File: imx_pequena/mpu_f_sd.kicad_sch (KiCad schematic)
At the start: 1 part, among them U1 MCIMX6Z0DVM09AB

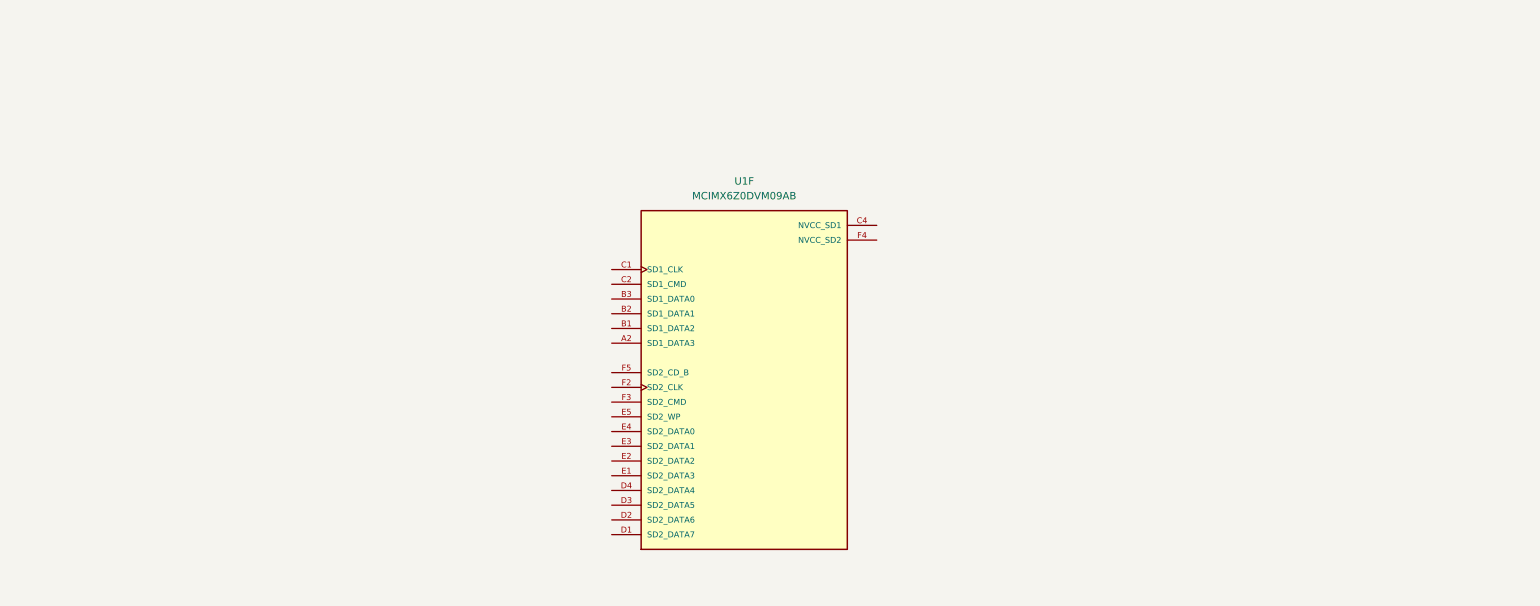
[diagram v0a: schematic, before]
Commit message: SD card + pinot files
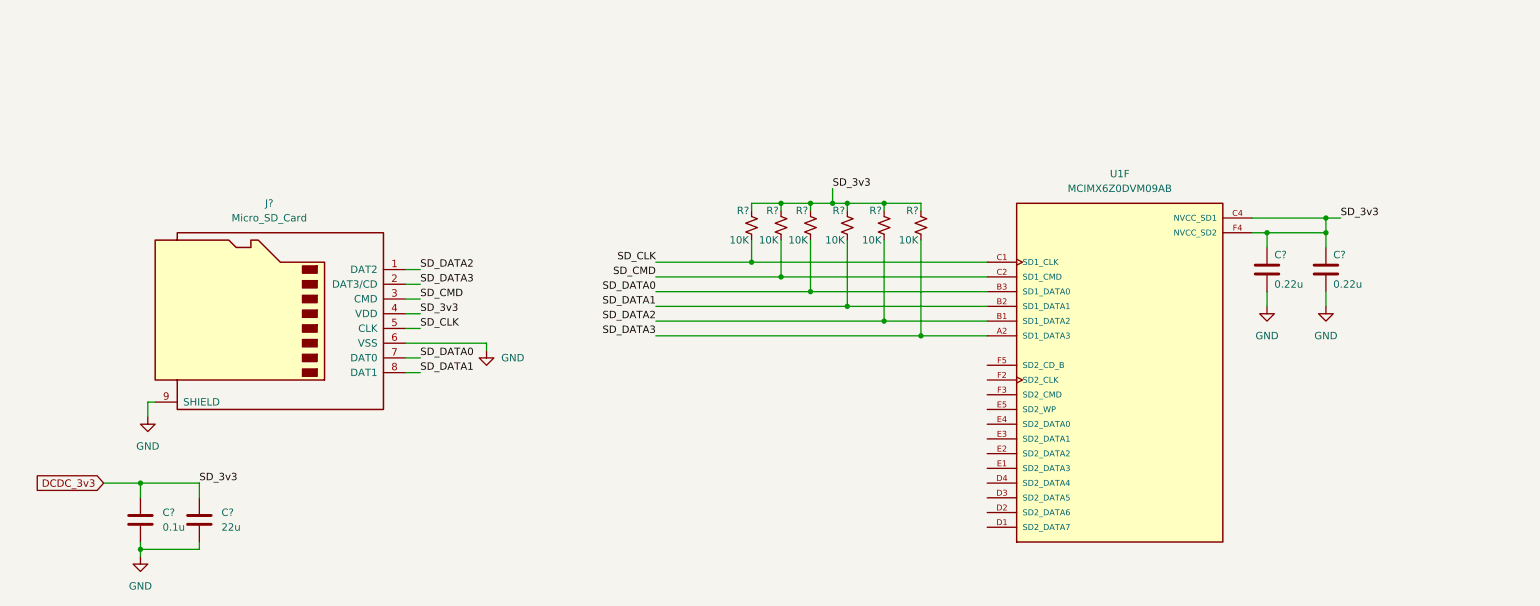
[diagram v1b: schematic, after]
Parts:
- added C? (x2): 0.22u, symbol Device:C
- added C?: 22u, symbol Device:C
- added C?: 0.1u, symbol Device:C
- added J?: Micro_SD_Card, symbol Connector:Micro_SD_Card
- added R? (x6): 10K, symbol Device:R_Small_US
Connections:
- net SD_DATA3: now reaches U1.A2 (SD1_DATA3)
- net SD_DATA3: now also J?.2 (DAT3/CD), R?.2
- net SD_DATA2: now reaches U1.B1 (SD1_DATA2)
- net SD_DATA2: now also J?.1 (DAT2), R?.2
- net SD_DATA1: now reaches U1.B2 (SD1_DATA1)
- net SD_DATA1: now also J?.8 (DAT1), R?.2
- net SD_DATA0: now reaches U1.B3 (SD1_DATA0)
- net SD_DATA0: now also J?.7 (DAT0), R?.2
- net SD_CLK: now reaches U1.C1 (SD1_CLK)
- net SD_CLK: now also J?.5 (CLK), R?.2
- net SD_CMD: now reaches U1.C2 (SD1_CMD)
- net SD_CMD: now also J?.3 (CMD), R?.2
- net DCDC_3v3: now reaches U1.C4 (NVCC_SD1)
- net DCDC_3v3: now also U1.F4 (NVCC_SD2), C?.1, C?.1, C?.1, C?.1, J?.4 (VDD), R?.1, R?.1, R?.1, R?.1, R?.1, R?.1
- new net GND: C?.2, C?.2, C?.2, C?.2, J?.6 (VSS), J?.9 (SHIELD)
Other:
- moved on the sheet: U1F

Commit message: Power Update
Added 3v3 and 1.35V switchers
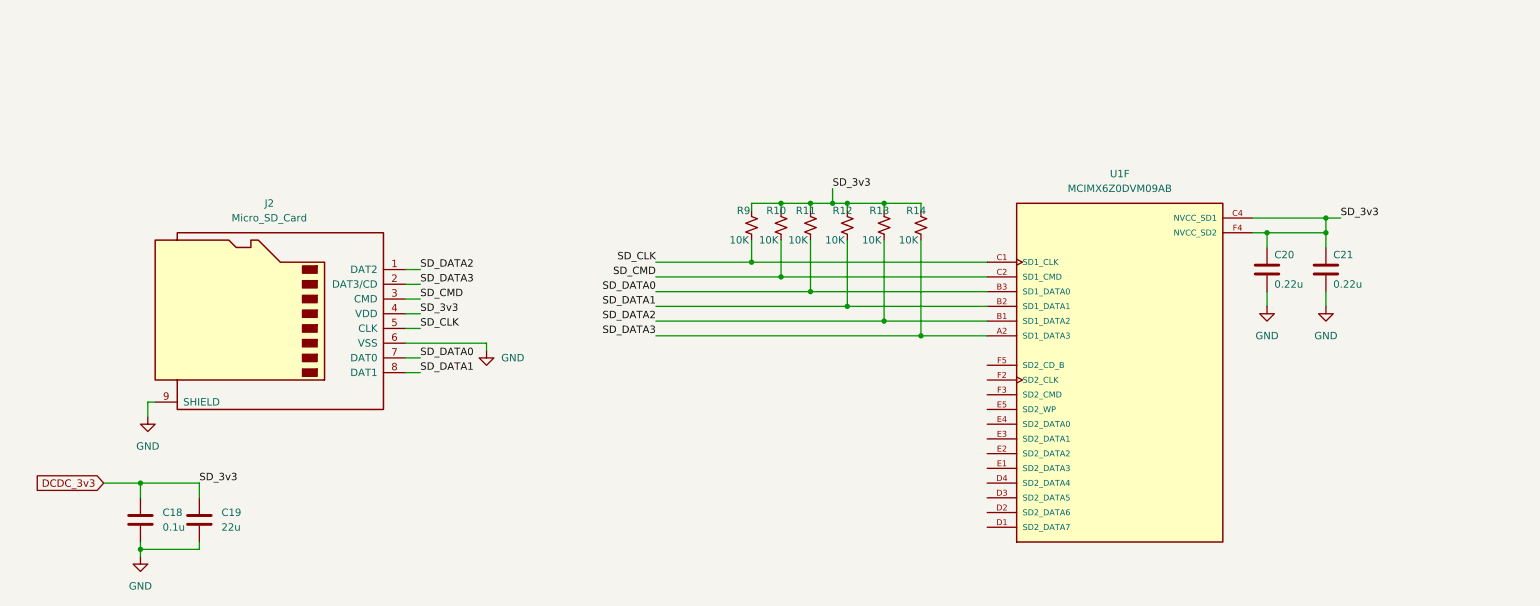
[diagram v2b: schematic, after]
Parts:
- gave numbers to parts that had none: 11
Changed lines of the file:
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@@
   (symbol (lib_id "Device:C") (at 245.11 62.23 0) (unit 1)
     (in_bom yes) (on_board yes)
-    (property "Reference" "C?" (id 0) (at 246.38 59.69 0)
+    (property "Reference" "C21" (id 0) (at 246.38 59.69 0)
       (effects (font (size 1.27 1.27)) (justify left))
     )
@@
   (symbol (lib_id "Device:R_Small_US") (at 156.21 54.61 0) (unit 1)
     (in_bom yes) (on_board yes)
-    (property "Reference" "R?" (id 0) (at 153.67 52.07 0)
+    (property "Reference" "R11" (id 0) (at 153.67 52.07 0)
       (effects (font (size 1.27 1.27)) (justify left))
     )
@@
   (symbol (lib_id "Device:R_Small_US") (at 146.05 54.61 0) (unit 1)
     (in_bom yes) (on_board yes)
-    (property "Reference" "R?" (id 0) (at 143.51 52.07 0)
+    (property "Reference" "R9" (id 0) (at 143.51 52.07 0)
       (effects (font (size 1.27 1.27)) (justify left))
     )
@@
   (symbol (lib_id "Device:R_Small_US") (at 175.26 54.61 0) (unit 1)
     (in_bom yes) (on_board yes)
-    (property "Reference" "R?" (id 0) (at 172.72 52.07 0)
+    (property "Reference" "R14" (id 0) (at 172.72 52.07 0)
       (effects (font (size 1.27 1.27)) (justify left))
     )
@@
   (symbol (lib_id "power:GND") (at 100.33 76.2 0) (unit 1)
     (in_bom yes) (on_board yes) (fields_autoplaced)
-    (property "Reference" "#PWR?" (id 0) (at 100.33 82.55 0)
+    (property "Reference" "#PWR0118" (id 0) (at 100.33 82.55 0)
       (effects (font (size 1.27 1.27)) hide)
     )
@@
   (symbol (lib_id "Device:C") (at 50.8 105.41 0) (unit 1)
     (in_bom yes) (on_board yes) (fields_autoplaced)
-    (property "Reference" "C?" (id 0) (at 54.61 104.1399 0)
+    (property "Reference" "C19" (id 0) (at 54.61 104.1399 0)
       (effects (font (size 1.27 1.27)) (justify left))
     )
@@
   (symbol (lib_id "Device:C") (at 234.95 62.23 0) (unit 1)
     (in_bom yes) (on_board yes)
-    (property "Reference" "C?" (id 0) (at 236.22 59.69 0)
+    (property "Reference" "C20" (id 0) (at 236.22 59.69 0)
       (effects (font (size 1.27 1.27)) (justify left))
     )
@@
   (symbol (lib_id "Connector:Micro_SD_Card") (at 63.5 69.85 0) (mirror y) (unit 1)
     (in_bom yes) (on_board yes) (fields_autoplaced)
-    (property "Reference" "J?" (id 0) (at 62.865 50.8 0))
+    (property "Reference" "J2" (id 0) (at 62.865 50.8 0))
     (property "Value" "Micro_SD_Card" (id 1) (at 62.865 53.34 0))
     (property "Footprint" "" (id 2) (at 34.29 62.23 0)
@@
   (symbol (lib_id "power:GND") (at 245.11 68.58 0) (unit 1)
     (in_bom yes) (on_board yes) (fields_autoplaced)
-    (property "Reference" "#PWR?" (id 0) (at 245.11 74.93 0)
+    (property "Reference" "#PWR0119" (id 0) (at 245.11 74.93 0)
       (effects (font (size 1.27 1.27)) hide)
     )
@@
   (symbol (lib_id "power:GND") (at 40.64 111.76 0) (unit 1)
     (in_bom yes) (on_board yes) (fields_autoplaced)
-    (property "Reference" "#PWR?" (id 0) (at 40.64 118.11 0)
+    (property "Reference" "#PWR0117" (id 0) (at 40.64 118.11 0)
       (effects (font (size 1.27 1.27)) hide)
     )
@@
   (symbol (lib_id "power:GND") (at 41.91 87.63 0) (unit 1)
     (in_bom yes) (on_board yes) (fields_autoplaced)
-    (property "Reference" "#PWR?" (id 0) (at 41.91 93.98 0)
+    (property "Reference" "#PWR0116" (id 0) (at 41.91 93.98 0)
       (effects (font (size 1.27 1.27)) hide)
     )
@@
   (symbol (lib_id "Device:C") (at 40.64 105.41 0) (unit 1)
     (in_bom yes) (on_board yes) (fields_autoplaced)
-    (property "Reference" "C?" (id 0) (at 44.45 104.1399 0)
+    (property "Reference" "C18" (id 0) (at 44.45 104.1399 0)
       (effects (font (size 1.27 1.27)) (justify left))
     )
@@
   (symbol (lib_id "power:GND") (at 234.95 68.58 0) (unit 1)
     (in_bom yes) (on_board yes) (fields_autoplaced)
-    (property "Reference" "#PWR?" (id 0) (at 234.95 74.93 0)
+    (property "Reference" "#PWR0120" (id 0) (at 234.95 74.93 0)
       (effects (font (size 1.27 1.27)) hide)
     )
@@
   (symbol (lib_id "Device:R_Small_US") (at 168.91 54.61 0) (unit 1)
     (in_bom yes) (on_board yes)
-    (property "Reference" "R?" (id 0) (at 166.37 52.07 0)
+    (property "Reference" "R13" (id 0) (at 166.37 52.07 0)
       (effects (font (size 1.27 1.27)) (justify left))
     )
@@
   (symbol (lib_id "Device:R_Small_US") (at 162.56 54.61 0) (unit 1)
     (in_bom yes) (on_board yes)
-    (property "Reference" "R?" (id 0) (at 160.02 52.07 0)
+    (property "Reference" "R12" (id 0) (at 160.02 52.07 0)
       (effects (font (size 1.27 1.27)) (justify left))
     )
@@
   (symbol (lib_id "Device:R_Small_US") (at 151.13 54.61 0) (unit 1)
     (in_bom yes) (on_board yes)
-    (property "Reference" "R?" (id 0) (at 148.59 52.07 0)
-      (effects (font (size 1.27 1.27)) (justify left))
-    )
+    (property "Reference" "R10" (id 0) (at 148.59 52.07 0)
+      (effects (font (size 1.27 1.27)) (justify left))
+    )

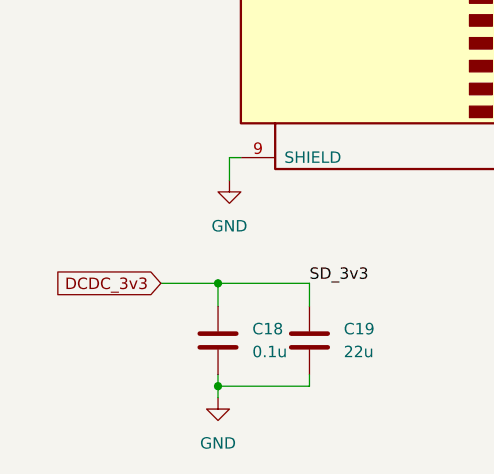
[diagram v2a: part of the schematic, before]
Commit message: Cleaned up NVCC pins
Added 3v3 connections + decoupling caps to NVcc pins
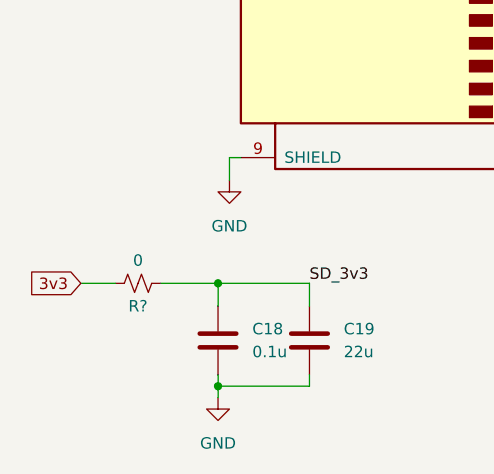
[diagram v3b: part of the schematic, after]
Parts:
- added R?: 0, symbol Device:R_Small_US
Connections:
- net DCDC_3v3 renamed SD_3v3
- net SD_3v3: now also R?.1
- new net 3v3: R?.2
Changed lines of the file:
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@@
+    (stroke (width 0) (type default) (color 0 0 0 0))
+  )
+  (wire (pts (xy 29.21 99.06) (xy 25.4 99.06))
     (stroke (width 0) (type default) (color 0 0 0 0))
   )
@@
     (effects (font (size 1.27 1.27)) (justify left bottom))
   )
-  (global_label "DCDC_3v3" (shape input) (at 34.29 99.06 180) (fields_autoplaced)
+  (global_label "3v3" (shape input) (at 25.4 99.06 180) (fields_autoplaced)
     (effects (font (size 1.27 1.27)) (justify right))
-    (property "Intersheet References" "${INTERSHEET_REFS}" (id 0) (at 22.4426 98.9806 0)
+    (property "Intersheet References" "${INTERSHEET_REFS}" (id 0) (at 19.6002 99.1394 0)
       (effects (font (size 1.27 1.27)) (justify right) hide)
     )
@@
     (pin "1")
   )
+  (symbol (lib_id "Device:R_Small_US") (at 31.75 99.06 270) (unit 1)
+    (in_bom yes) (on_board yes)
+    (property "Reference" "R?" (id 0) (at 31.75 101.6 90))
+    (property "Value" "0" (id 1) (at 31.75 96.52 90))
+    (property "Footprint" "" (id 2) (at 31.75 99.06 0)
+      (effects (font (size 1.27 1.27)) hide)
+    )
+    (property "Datasheet" "~" (id 3) (at 31.75 99.06 0)
+      (effects (font (size 1.27 1.27)) hide)
+    )
+    (pin "1")
+    (pin "2")
+  )
   (symbol (lib_id "Device:R_Small_US") (at 168.91 54.61 0) (unit 1)
